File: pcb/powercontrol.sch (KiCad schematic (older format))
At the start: 10 parts, among them P2 CONN_01X02, Q1 AO3401, Q2 AO3401, Q3 2N7002, U2 DMMT5401

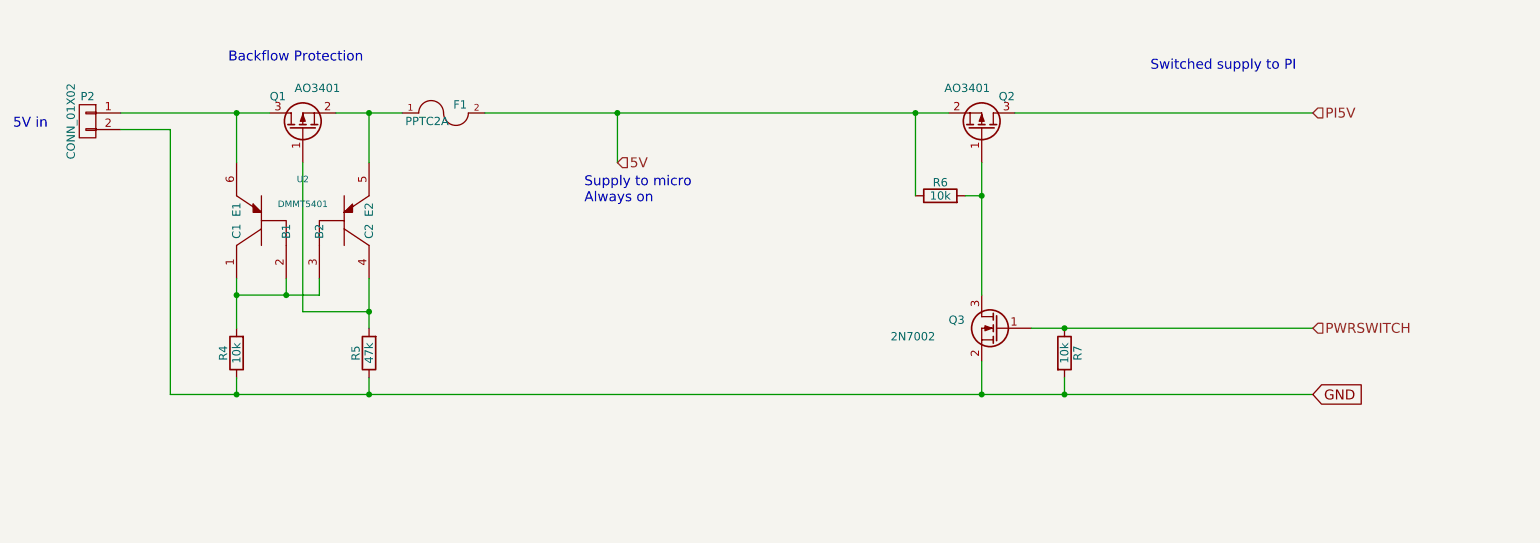
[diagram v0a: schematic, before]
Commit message: added SPI flash and connections for STM32 to control the sensors
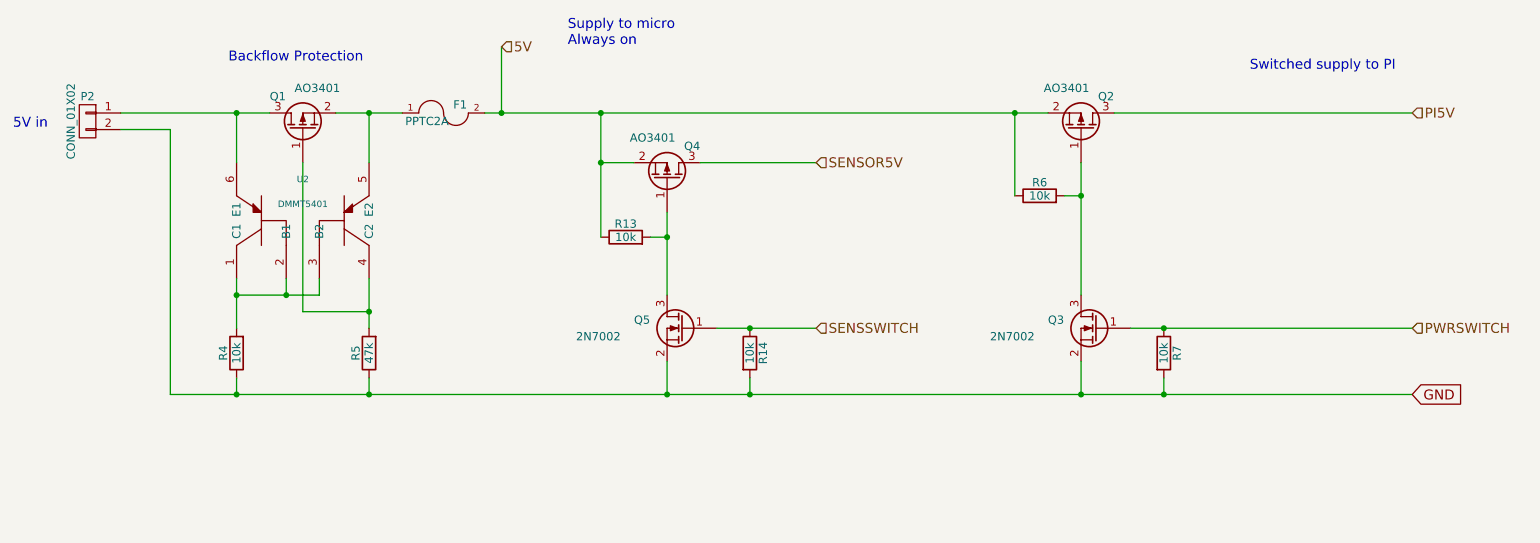
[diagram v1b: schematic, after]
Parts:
- added Q4: AO3401, TO_SOT_Packages_SMD:SOT-23, symbol Q_PMOS_GSD
- added Q5: 2N7002, TO_SOT_Packages_SMD:SOT-23, symbol Q_NMOS_GSD
- added R13, R14: 10k, Resistors_SMD:R_0805, symbol R
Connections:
- net 5V: now also Q4.2 (S), R13.1
- net GND: now also Q5.2 (S), R14.2
- new net: Q4.1 (G), Q5.3 (D), R13.2
- new net SENSOR5V: Q4.3 (D)
- new net SENSSWITCH: Q5.1 (G), R14.1
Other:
- moved on the sheet: Q2, Q3, R6, R7
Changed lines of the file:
@@
 	1    0    0    -1
 $EndComp
-Text GLabel 9400 4500 2    60   Input ~ 0
+Text GLabel 10000 4500 2    60   Input ~ 0
 GND
 $Comp
 L Q_PMOS_GSD Q2
 U 1 1 57B3250D
-P 7400 2900
-F 0 "Q2" V 7600 3100 50  0000 R CNN
-F 1 "AO3401" V 7650 2950 50  0000 R CNN
-F 2 "TO_SOT_Packages_SMD:SOT-23" H 7600 3000 50  0001 C CNN
-F 3 "" H 7400 2900 50  0000 C CNN
-	1    7400 2900
+P 8000 2900
+F 0 "Q2" V 8200 3100 50  0000 R CNN
+F 1 "AO3401" V 8250 2950 50  0000 R CNN
+F 2 "TO_SOT_Packages_SMD:SOT-23" H 8200 3000 50  0001 C CNN
+F 3 "" H 8000 2900 50  0000 C CNN
+	1    8000 2900
 	0    1    -1   0
 $EndComp
@@
 L R R6
 U 1 1 57B3260E
-P 7150 3300
-F 0 "R6" V 7230 3300 50  0000 C CNN
-F 1 "10k" V 7150 3300 50  0000 C CNN
-F 2 "Resistors_SMD:R_0805" V 7080 3300 50  0001 C CNN
-F 3 "" H 7150 3300 50  0000 C CNN
-	1    7150 3300
+P 7750 3300
+F 0 "R6" V 7830 3300 50  0000 C CNN
+F 1 "10k" V 7750 3300 50  0000 C CNN
+F 2 "Resistors_SMD:R_0805" V 7680 3300 50  0001 C CNN
+F 3 "" H 7750 3300 50  0000 C CNN
+	1    7750 3300
 	0    -1   -1   0
 $EndComp
@@
 L Q_NMOS_GSD Q3
 U 1 1 57B32914
-P 7500 4100
-F 0 "Q3" H 7800 4150 50  0000 R CNN
-F 1 "2N7002" H 8150 4050 50  0000 R CNN
-F 2 "TO_SOT_Packages_SMD:SOT-23" H 7700 4200 50  0001 C CNN
-F 3 "" H 7500 4100 50  0000 C CNN
-	1    7500 4100
+P 8100 4100
+F 0 "Q3" H 8400 4150 50  0000 R CNN
+F 1 "2N7002" H 8750 4050 50  0000 R CNN
+F 2 "TO_SOT_Packages_SMD:SOT-23" H 8300 4200 50  0001 C CNN
+F 3 "" H 8100 4100 50  0000 C CNN
+	1    8100 4100
 	-1   0    0    -1
 $EndComp
@@
 L R R7
 U 1 1 57B32BA6
-P 7900 4250
-F 0 "R7" V 7980 4250 50  0000 C CNN
-F 1 "10k" V 7900 4250 50  0000 C CNN
-F 2 "Resistors_SMD:R_0805" V 7830 4250 50  0001 C CNN
-F 3 "" H 7900 4250 50  0000 C CNN
-	1    7900 4250
+P 8500 4250
+F 0 "R7" V 8580 4250 50  0000 C CNN
+F 1 "10k" V 8500 4250 50  0000 C CNN
+F 2 "Resistors_SMD:R_0805" V 8430 4250 50  0001 C CNN
+F 3 "" H 8500 4250 50  0000 C CNN
+	1    8500 4250
 	1    0    0    -1
 $EndComp
@@
 	3700 3800 3700 4100
 Wire Wire Line
-	3400 3800 3400 3900
+	3400 3900 3400 3800
 Wire Wire Line
-	3400 3900 2900 3900
+	2900 3900 3400 3900
 Wire Wire Line
 	2900 3800 2900 4100
@@
 	3500 2800 3900 2800
 Wire Wire Line
-	2500 4500 9400 4500
+	2500 4500 10000 4500
 Wire Wire Line
-	7000 2800 7000 3300
+	7600 2800 7600 3300
 Wire Wire Line
-	4400 2800 7200 2800
+	4400 2800 7800 2800
 Wire Wire Line
-	7300 3300 7400 3300
+	7900 3300 8000 3300
 Wire Wire Line
-	7400 3100 7400 3900
-Connection ~ 7400 3300
+	8000 3100 8000 3900
+Connection ~ 8000 3300
 Wire Wire Line
-	7400 4500 7400 4300
+	8000 4500 8000 4300
 Wire Wire Line
-	7700 4100 9400 4100
+	8300 4100 10000 4100
 Wire Wire Line
-	7900 4500 7900 4400
-Connection ~ 7400 4500
-Connection ~ 7000 2800
+	8500 4500 8500 4400
+Connection ~ 8000 4500
+Connection ~ 7600 2800
 Wire Wire Line
-	7600 2800 9400 2800
-Connection ~ 7900 4500
-Connection ~ 5200 2800
-Text Notes 5000 3350 0    60   ~ 0
+	8200 2800 10000 2800
+Connection ~ 8500 4500
+Connection ~ 4500 2800
+Text Notes 4900 2400 0    60   ~ 0
 Supply to micro\nAlways on
-Text Notes 9300 2550 2    60   ~ 0
+Text Notes 9900 2550 2    60   ~ 0
 Switched supply to PI
-Text HLabel 9400 4100 2    60   Input ~ 0
+Text HLabel 10000 4100 2    60   Input ~ 0
 PWRSWITCH
-Connection ~ 7900 4100
+Connection ~ 8500 4100
+Text HLabel 10000 2800 2    60   Input ~ 0
+PI5V
+Text HLabel 4500 2400 2    60   Input ~ 0
+5V
+$Comp
+L R R13
+U 1 1 57B5F826
+P 5250 3550
+F 0 "R13" V 5330 3550 50  0000 C CNN
+F 1 "10k" V 5250 3550 50  0000 C CNN
+F 2 "Resistors_SMD:R_0805" V 5180 3550 50  0001 C CNN
+F 3 "" H 5250 3550 50  0000 C CNN
+	1    5250 3550
+	0    -1   -1   0
+$EndComp
+$Comp
+L Q_NMOS_GSD Q5
+U 1 1 57B5F82C
+P 5600 4100
+F 0 "Q5" H 5900 4150 50  0000 R CNN
+F 1 "2N7002" H 6250 4050 50  0000 R CNN
+F 2 "TO_SOT_Packages_SMD:SOT-23" H 5800 4200 50  0001 C CNN
+F 3 "" H 5600 4100 50  0000 C CNN
+	1    5600 4100
+	-1   0    0    -1
+$EndComp
+$Comp
+L R R14
+U 1 1 57B5F832
+P 6000 4250
+F 0 "R14" V 6080 4250 50  0000 C CNN
+F 1 "10k" V 6000 4250 50  0000 C CNN
+F 2 "Resistors_SMD:R_0805" V 5930 4250 50  0001 C CNN
+F 3 "" H 6000 4250 50  0000 C CNN
+	1    6000 4250
+	1    0    0    -1
+$EndComp
 Wire Wire Line
-	5200 2800 5200 3100
-Text HLabel 9400 2800 2    60   Input ~ 0
-PI5V
-Text HLabel 5200 3100 2    60   Input ~ 0
-5V
+	5100 2800 5100 3550
+Wire Wire Line
+	5400 3550 5500 3550
+Connection ~ 5500 3550
+Wire Wire Line
+	5500 4500 5500 4300
+Wire Wire Line
+	6000 4500 6000 4400
+Connection ~ 5500 4500
+Connection ~ 6000 4500
+Connection ~ 6000 4100
+$Comp
+L Q_PMOS_GSD Q4
+U 1 1 57B5F820
+P 5500 3200
+F 0 "Q4" V 5700 3400 50  0000 R CNN
+F 1 "AO3401" V 5750 3250 50  0000 R CNN
+F 2 "TO_SOT_Packages_SMD:SOT-23" H 5700 3300 50  0001 C CNN
+F 3 "" H 5500 3200 50  0000 C CNN
+	1    5500 3200
+	0    1    -1   0
+$EndComp
+Connection ~ 5100 2800
+Wire Wire Line
+	5500 3400 5500 3900
+Text HLabel 6400 4100 2    60   Input ~ 0
+SENSSWITCH
+Wire Wire Line
+	5300 3100 5100 3100
+Connection ~ 5100 3100
+Wire Wire Line
+	5700 3100 6400 3100
+Text HLabel 6400 3100 2    60   Input ~ 0
+SENSOR5V
+Wire Wire Line
+	6400 4100 5800 4100
+Wire Wire Line
+	4500 2800 4500 2400
 $EndSCHEMATC

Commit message: draft component placement for PCB
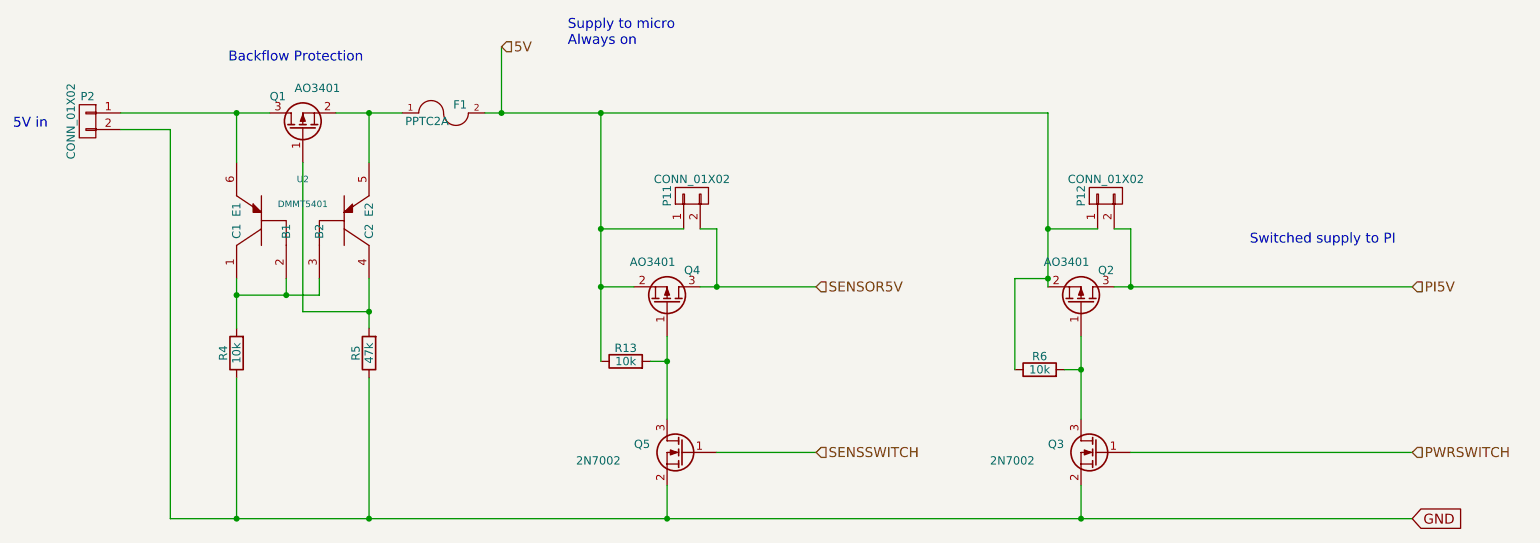
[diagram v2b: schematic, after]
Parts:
- removed R14, R7: 10k, Resistors_SMD:R_0805, symbol R
- added P11, P12: CONN_01X02, Pin_Headers:Pin_Header_Straight_1x02, symbol CONN_01X02
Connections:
- net 5V: now also P11.1 (P1), P12.1 (P1)
- net PI5V: now also P12.2 (P2)
- net SENSOR5V: now also P11.2 (P2)
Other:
- moved on the sheet: Q2, Q3, Q4, Q5, R13, R6
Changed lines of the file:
@@
 	1    0    0    -1
 $EndComp
-Text GLabel 10000 4500 2    60   Input ~ 0
+Text GLabel 10000 5250 2    60   Input ~ 0
 GND
 $Comp
 L Q_PMOS_GSD Q2
 U 1 1 57B3250D
-P 8000 2900
-F 0 "Q2" V 8200 3100 50  0000 R CNN
-F 1 "AO3401" V 8250 2950 50  0000 R CNN
-F 2 "TO_SOT_Packages_SMD:SOT-23" H 8200 3000 50  0001 C CNN
-F 3 "" H 8000 2900 50  0000 C CNN
-	1    8000 2900
+P 8000 3950
+F 0 "Q2" V 8200 4150 50  0000 R CNN
+F 1 "AO3401" V 8250 4000 50  0000 R CNN
+F 2 "TO_SOT_Packages_SMD:SOT-23" H 8200 4050 50  0001 C CNN
+F 3 "" H 8000 3950 50  0000 C CNN
+	1    8000 3950
 	0    1    -1   0
 $EndComp
@@
 L R R6
 U 1 1 57B3260E
-P 7750 3300
-F 0 "R6" V 7830 3300 50  0000 C CNN
-F 1 "10k" V 7750 3300 50  0000 C CNN
-F 2 "Resistors_SMD:R_0805" V 7680 3300 50  0001 C CNN
-F 3 "" H 7750 3300 50  0000 C CNN
-	1    7750 3300
+P 7750 4350
+F 0 "R6" V 7830 4350 50  0000 C CNN
+F 1 "10k" V 7750 4350 50  0000 C CNN
+F 2 "Resistors_SMD:R_0805" V 7680 4350 50  0001 C CNN
+F 3 "" H 7750 4350 50  0000 C CNN
+	1    7750 4350
 	0    -1   -1   0
 $EndComp
@@
 L Q_NMOS_GSD Q3
 U 1 1 57B32914
-P 8100 4100
-F 0 "Q3" H 8400 4150 50  0000 R CNN
-F 1 "2N7002" H 8750 4050 50  0000 R CNN
-F 2 "TO_SOT_Packages_SMD:SOT-23" H 8300 4200 50  0001 C CNN
-F 3 "" H 8100 4100 50  0000 C CNN
-	1    8100 4100
+P 8100 4850
+F 0 "Q3" H 8400 4900 50  0000 R CNN
+F 1 "2N7002" H 8750 4800 50  0000 R CNN
+F 2 "TO_SOT_Packages_SMD:SOT-23" H 8300 4950 50  0001 C CNN
+F 3 "" H 8100 4850 50  0000 C CNN
+	1    8100 4850
 	-1   0    0    -1
 $EndComp
-$Comp
-L R R7
-U 1 1 57B32BA6
-P 8500 4250
-F 0 "R7" V 8580 4250 50  0000 C CNN
-F 1 "10k" V 8500 4250 50  0000 C CNN
-F 2 "Resistors_SMD:R_0805" V 8430 4250 50  0001 C CNN
-F 3 "" H 8500 4250 50  0000 C CNN
-	1    8500 4250
-	1    0    0    -1
+Text Notes 4900 2400 0    60   ~ 0
+Supply to micro\nAlways on
+Text Notes 9900 3600 2    60   ~ 0
+Switched supply to PI
+Text HLabel 10000 4850 2    60   Input ~ 0
+PWRSWITCH
+Text HLabel 10000 3850 2    60   Input ~ 0
+PI5V
+Text HLabel 4500 2400 2    60   Input ~ 0
+5V
+$Comp
+L R R13
+U 1 1 57B5F826
+P 5250 4300
+F 0 "R13" V 5330 4300 50  0000 C CNN
+F 1 "10k" V 5250 4300 50  0000 C CNN
+F 2 "Resistors_SMD:R_0805" V 5180 4300 50  0001 C CNN
+F 3 "" H 5250 4300 50  0000 C CNN
+	1    5250 4300
+	0    -1   -1   0
+$EndComp
+$Comp
+L Q_NMOS_GSD Q5
+U 1 1 57B5F82C
+P 5600 4850
+F 0 "Q5" H 5900 4900 50  0000 R CNN
+F 1 "2N7002" H 6250 4800 50  0000 R CNN
+F 2 "TO_SOT_Packages_SMD:SOT-23" H 5800 4950 50  0001 C CNN
+F 3 "" H 5600 4850 50  0000 C CNN
+	1    5600 4850
+	-1   0    0    -1
+$EndComp
+$Comp
+L Q_PMOS_GSD Q4
+U 1 1 57B5F820
+P 5500 3950
+F 0 "Q4" V 5700 4150 50  0000 R CNN
+F 1 "AO3401" V 5750 4000 50  0000 R CNN
+F 2 "TO_SOT_Packages_SMD:SOT-23" H 5700 4050 50  0001 C CNN
+F 3 "" H 5500 3950 50  0000 C CNN
+	1    5500 3950
+	0    1    -1   0
+$EndComp
+Text HLabel 6400 4850 2    60   Input ~ 0
+SENSSWITCH
+Text HLabel 6400 3850 2    60   Input ~ 0
+SENSOR5V
+$Comp
+L CONN_01X02 P12
+U 1 1 5808AFCC
+P 8150 3300
+F 0 "P12" H 8150 3450 50  0000 C CNN
+F 1 "CONN_01X02" V 8250 3300 50  0000 C CNN
+F 2 "Pin_Headers:Pin_Header_Straight_1x02" H 8150 3300 50  0001 C CNN
+F 3 "" H 8150 3300 50  0000 C CNN
+	1    8150 3300
+	0    -1   -1   0
 $EndComp
 Wire Wire Line
@@
 Connection ~ 3700 4000
 Wire Wire Line
-	2900 4400 2900 4500
-Wire Wire Line
-	3700 4500 3700 4400
-Connection ~ 3700 4500
+	2900 4400 2900 5250
+Wire Wire Line
+	3700 4400 3700 5250
+Connection ~ 3700 5250
 Wire Wire Line
 	2200 2900 2500 2900
-Connection ~ 2900 4500
+Connection ~ 2900 5250
 Wire Wire Line
 	2900 2800 2900 3100
@@
 	3300 3100 3300 4000
 Wire Wire Line
-	2500 2900 2500 4500
+	2500 2900 2500 5250
 Wire Wire Line
 	3500 2800 3900 2800
 Wire Wire Line
-	2500 4500 10000 4500
-Wire Wire Line
-	7600 2800 7600 3300
+	2500 5250 10000 5250
 Wire Wire Line
 	4400 2800 7800 2800
 Wire Wire Line
-	7900 3300 8000 3300
-Wire Wire Line
-	8000 3100 8000 3900
-Connection ~ 8000 3300
-Wire Wire Line
-	8000 4500 8000 4300
-Wire Wire Line
-	8300 4100 10000 4100
-Wire Wire Line
-	8500 4500 8500 4400
-Connection ~ 8000 4500
-Connection ~ 7600 2800
-Wire Wire Line
-	8200 2800 10000 2800
-Connection ~ 8500 4500
+	7900 4350 8000 4350
+Connection ~ 8000 4350
+Wire Wire Line
+	8000 5250 8000 5050
+Wire Wire Line
+	8300 4850 10000 4850
+Connection ~ 8000 5250
+Wire Wire Line
+	8200 3850 10000 3850
 Connection ~ 4500 2800
-Text Notes 4900 2400 0    60   ~ 0
-Supply to micro\nAlways on
-Text Notes 9900 2550 2    60   ~ 0
-Switched supply to PI
-Text HLabel 10000 4100 2    60   Input ~ 0
-PWRSWITCH
-Connection ~ 8500 4100
-Text HLabel 10000 2800 2    60   Input ~ 0
-PI5V
-Text HLabel 4500 2400 2    60   Input ~ 0
-5V
-$Comp
-L R R13
-U 1 1 57B5F826
-P 5250 3550
-F 0 "R13" V 5330 3550 50  0000 C CNN
-F 1 "10k" V 5250 3550 50  0000 C CNN
-F 2 "Resistors_SMD:R_0805" V 5180 3550 50  0001 C CNN
-F 3 "" H 5250 3550 50  0000 C CNN
-	1    5250 3550
-	0    -1   -1   0
-$EndComp
-$Comp
-L Q_NMOS_GSD Q5
-U 1 1 57B5F82C
-P 5600 4100
-F 0 "Q5" H 5900 4150 50  0000 R CNN
-F 1 "2N7002" H 6250 4050 50  0000 R CNN
-F 2 "TO_SOT_Packages_SMD:SOT-23" H 5800 4200 50  0001 C CNN
-F 3 "" H 5600 4100 50  0000 C CNN
-	1    5600 4100
-	-1   0    0    -1
-$EndComp
-$Comp
-L R R14
-U 1 1 57B5F832
-P 6000 4250
-F 0 "R14" V 6080 4250 50  0000 C CNN
-F 1 "10k" V 6000 4250 50  0000 C CNN
-F 2 "Resistors_SMD:R_0805" V 5930 4250 50  0001 C CNN
-F 3 "" H 6000 4250 50  0000 C CNN
-	1    6000 4250
-	1    0    0    -1
-$EndComp
-Wire Wire Line
-	5100 2800 5100 3550
-Wire Wire Line
-	5400 3550 5500 3550
-Connection ~ 5500 3550
-Wire Wire Line
-	5500 4500 5500 4300
-Wire Wire Line
-	6000 4500 6000 4400
-Connection ~ 5500 4500
-Connection ~ 6000 4500
-Connection ~ 6000 4100
-$Comp
-L Q_PMOS_GSD Q4
-U 1 1 57B5F820
-P 5500 3200
-F 0 "Q4" V 5700 3400 50  0000 R CNN
-F 1 "AO3401" V 5750 3250 50  0000 R CNN
-F 2 "TO_SOT_Packages_SMD:SOT-23" H 5700 3300 50  0001 C CNN
-F 3 "" H 5500 3200 50  0000 C CNN
-	1    5500 3200
-	0    1    -1   0
-$EndComp
+Wire Wire Line
+	5100 2800 5100 4300
+Wire Wire Line
+	5400 4300 5500 4300
+Connection ~ 5500 4300
+Wire Wire Line
+	5500 5250 5500 5050
+Connection ~ 5500 5250
 Connection ~ 5100 2800
 Wire Wire Line
-	5500 3400 5500 3900
-Text HLabel 6400 4100 2    60   Input ~ 0
-SENSSWITCH
-Wire Wire Line
-	5300 3100 5100 3100
-Connection ~ 5100 3100
-Wire Wire Line
-	5700 3100 6400 3100
-Text HLabel 6400 3100 2    60   Input ~ 0
-SENSOR5V
-Wire Wire Line
-	6400 4100 5800 4100
+	5500 4150 5500 4650
+Wire Wire Line
+	5300 3850 5100 3850
+Connection ~ 5100 3850
+Wire Wire Line
+	5700 3850 6400 3850
+Wire Wire Line
+	6400 4850 5800 4850
 Wire Wire Line
 	4500 2800 4500 2400
+Wire Wire Line
+	7800 2800 7800 3850
+Wire Wire Line
+	7800 3800 7600 3800
+Wire Wire Line
+	7600 3800 7600 4350
+Connection ~ 7800 3800
+Wire Wire Line
+	8000 4650 8000 4150
+Wire Wire Line
+	7800 3500 8100 3500
+Connection ~ 7800 3500
+Wire Wire Line
+	8200 3500 8300 3500
+Wire Wire Line
+	8300 3500 8300 3850
+Connection ~ 8300 3850
+$Comp
+L CONN_01X02 P11
+U 1 1 5808B7C5
+P 5650 3300
+F 0 "P11" H 5650 3450 50  0000 C CNN
+F 1 "CONN_01X02" V 5750 3300 50  0000 C CNN
+F 2 "Pin_Headers:Pin_Header_Straight_1x02" H 5650 3300 50  0001 C CNN
+F 3 "" H 5650 3300 50  0000 C CNN
+	1    5650 3300
+	0    -1   -1   0
+$EndComp
+Wire Wire Line
+	5100 3500 5600 3500
+Connection ~ 5100 3500
+Wire Wire Line
+	5700 3500 5800 3500
+Wire Wire Line
+	5800 3500 5800 3850
+Connection ~ 5800 3850
 $EndSCHEMATC
